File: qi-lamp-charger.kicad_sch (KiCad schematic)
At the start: 80 parts, among them J1 Conn_01x02, J2 Conn_01x02, J3 Conn_01x02, J4 Conn_01x06, J5 Conn_01x03, Q1 Q_PMOS_GDS, U1 SLG5NV1430V, U2 BQ51050BYFP, U3 ESP-12E

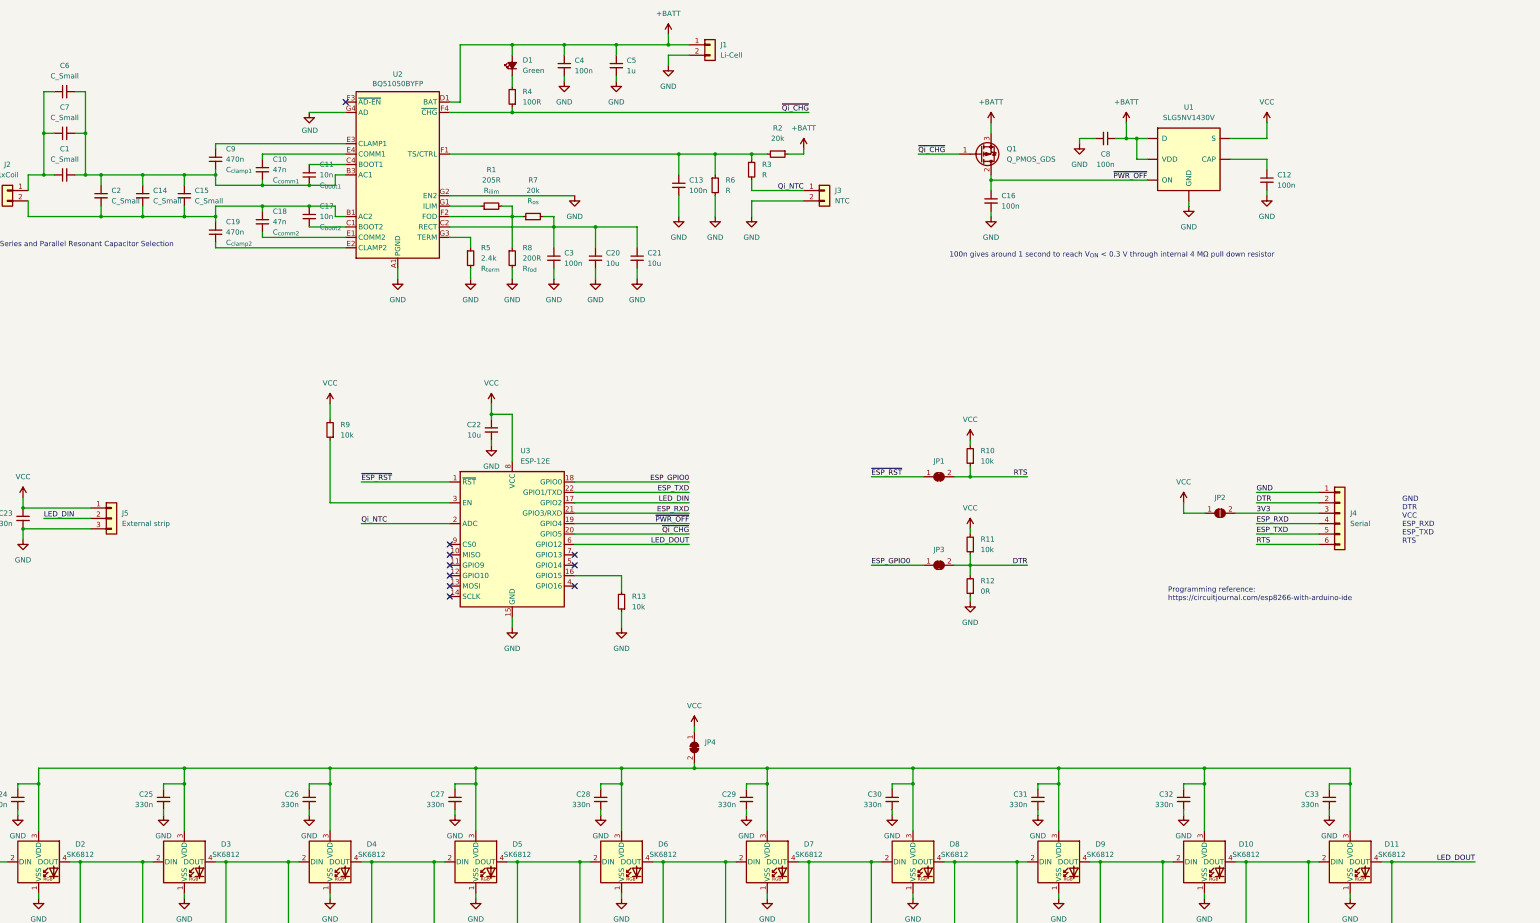
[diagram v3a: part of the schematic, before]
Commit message: Redraw Button/DTR/GPIO0 complex & assign footprints
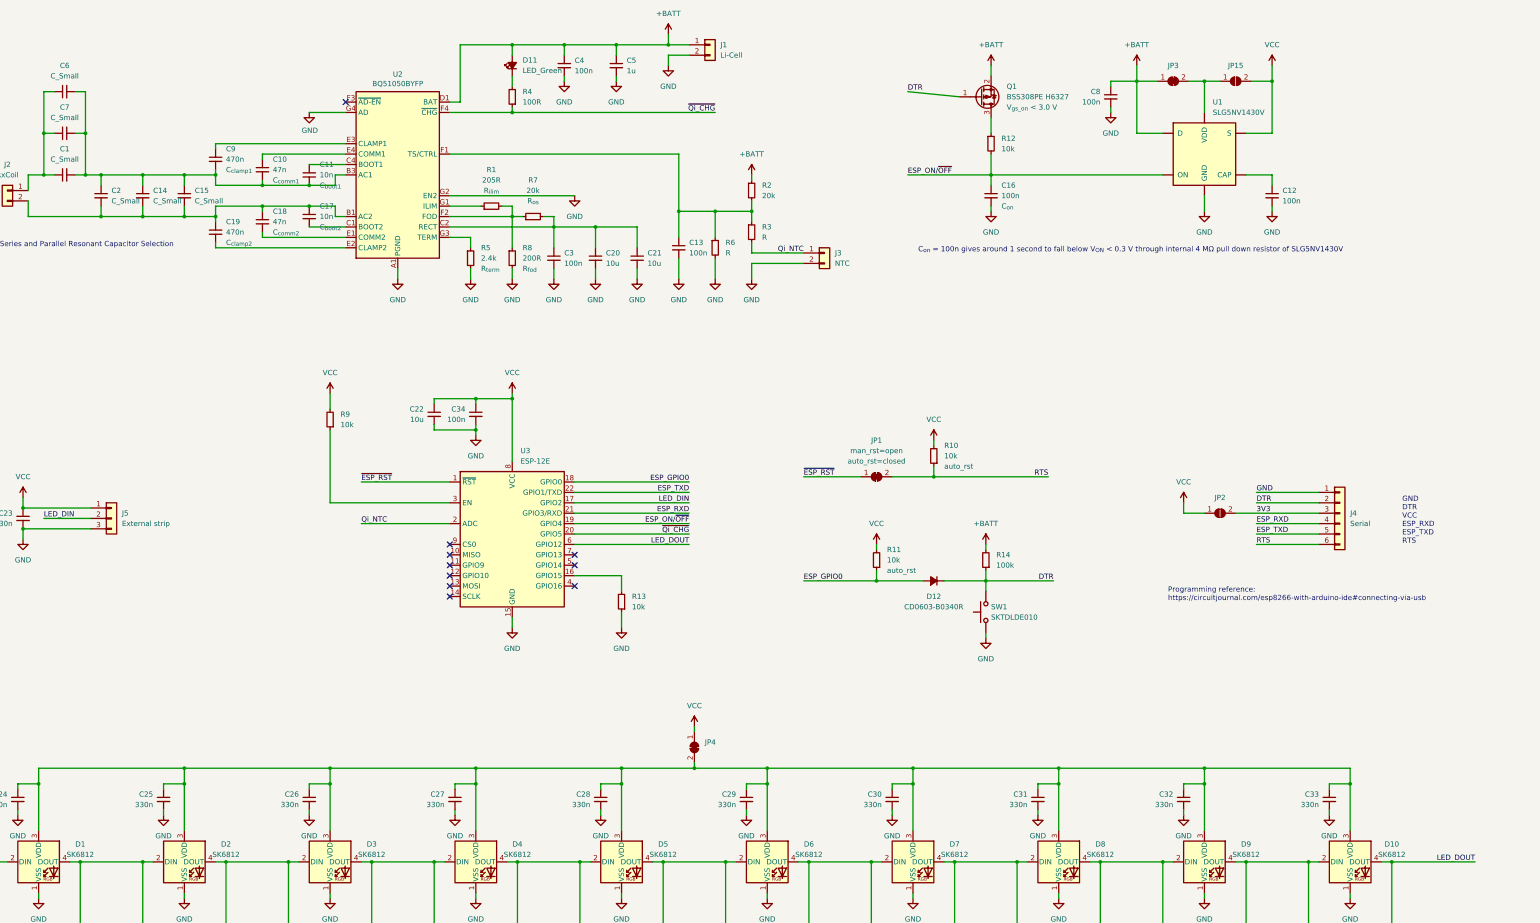
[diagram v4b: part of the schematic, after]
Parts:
- added C34: 100n, Capacitor_SMD:C_0603_1608Metric, symbol Device:C_Small
- added D12: CD0603-B0340R, Diode_SMD:D_0603_1608Metric, symbol Device:D_Small_Filled
- added JP15: SolderJumper_2_Open, Jumper:SolderJumper-2_P1.3mm_Open_RoundedPad1.0x1.5mm, symbol Jumper:SolderJumper_2_Open
- added R14: 100k, Resistor_SMD:R_0603_1608Metric, symbol Device:R_Small
- added SW1: SKTDLDE010, Kharars-KiCAD-lib:SKTDLDE010, symbol Switch:SW_Push
- C16: silk_text (none) -> C_{on}
- D11: renamed from D1; value Green -> LED_Green
- JP1: Rating (none) -> auto_rst=closed; silk_text (none) -> man_rst=open
- Q1: value Q_PMOS_GDS -> BSS308PE H6327; footprint (none) -> Package_TO_SOT_SMD:SOT-23; symbol Device:Q_PMOS_GDS -> Device:Q_PMOS_GSD; Rating (none) -> V_{gs_on} < 3.0 V
- R12: value 0R -> 10k; fit_field man_rst -> (none)
- U1: footprint (none) -> Kharars-KiCAD-lib:TDFN-8_1.5x2.0mm_P0.5mm (Fused Lead)
- renumbered D2 to D1, D11 to D10, D3 to D2, D4 to D3, D5 to D4, D6 to D5, D7 to D6, D8 to D7, D9 to D8, D10 to D9
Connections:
- net +BATT: now also JP3.1 (A), Q1.2 (S), R14.2; no longer Q1.3 (S), U1.1 (VDD)
- net DTR: now also Q1.1 (G), D12.1 (K), R14.1, SW1.2; no longer JP3.2 (B), R11.1, R12.2
- net ESP_GPIO0: now also R11.1, D12.2 (A); no longer JP3.1 (A)
- net GND: now also C34.2, SW1.1; no longer R12.1
- net VCC: now also C34.1, JP15.2 (B)
- net ~{Qi_CHG}: no longer Q1.1 (G)
- net ~{PWR_OFF} renamed ESP_ON/~{OFF}
- net ESP_ON/~{OFF}: now also R12.2; no longer Q1.2 (D)
- new net: JP15.1 (A), JP3.2 (B), U1.1 (VDD)
- new net: Q1.3 (D), R12.1
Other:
- note added: "C_{on} = 100n gives around 1 second to fall below V_{ON} < 0.3 V through internal 4 MΩ pull down resistor of SLG5NV1430V"
- note added: "Programming reference: https://circuitjournal.com/esp8266-with-arduino-ide#connecting-via-usb"
- note removed: "100n gives around 1 second to reach V_{ON} < 0.3 V through internal 4 MΩ pull down resistor"
- note removed: "Programming reference: https://circuitjournal.com/esp8266-with-arduino-ide"
- company: (none) -> Step 7 ApS
- title: (none) -> Main schematic
- moved on the sheet: C12, C13, C16, C22, C8, J3, Q1, R10, R11, R2, R3, R6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

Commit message: Layout proposal 1
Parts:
- C13: Name (none) -> C_{3}
- SW1: symbol Switch:SW_Push -> Kharars-KiCAD-lib:SW_Push
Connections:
- net GND: now also SW1.3
- net LED_VCC: now reaches C24.1, C25.1, C26.1, C27.1, C28.1, C29.1, C30.1, C31.1, C32.1, C33.1, D1.3 (VDD), D10.3 (VDD), D2.3 (VDD), D3.3 (VDD), D4.3 (VDD), D5.3 (VDD), D6.3 (VDD), D7.3 (VDD), D8.3 (VDD), D9.3 (VDD), JP4.2 (B)
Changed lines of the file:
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@@
     (stroke (width 0) (type default) (color 0 0 0 0))
   )
+  (wire (pts (xy 269.24 162.56) (xy 269.24 168.91))
+    (stroke (width 0) (type default) (color 0 0 0 0))
+  )
   (wire (pts (xy 344.17 135.89) (xy 359.41 135.89))
     (stroke (width 0) (type default) (color 0 0 0 0))
@@
     (stroke (width 0) (type default) (color 0 0 0 0))
   )
-  (wire (pts (xy 259.08 35.56) (xy 271.78 36.83))
+  (wire (pts (xy 259.08 36.83) (xy 271.78 36.83))
     (stroke (width 0) (type default) (color 0 0 0 0))
   )
@@
     (stroke (width 0) (type default) (color 0 0 0 0))
   )
+  (wire (pts (xy 273.05 162.56) (xy 269.24 162.56))
+    (stroke (width 0) (type default) (color 0 0 0 0))
+  )
   (wire (pts (xy 203.2 50.8) (xy 203.2 64.77))
     (stroke (width 0) (type default) (color 0 0 0 0))
@@
     (effects (font (size 1.27 1.27)) (justify left bottom))
   )
-  (label "DTR" (at 259.08 35.56 0)
+  (label "DTR" (at 259.08 36.83 0)
     (effects (font (size 1.27 1.27)) (justify left bottom))
   )
@@
     (effects (font (size 1.27 1.27)) (justify right bottom))
   )
+  (label "LED_VCC" (at 213.36 200.66 0)
+    (effects (font (size 1.27 1.27)) (justify left bottom))
+  )
   (label "~{Qi_CHG}" (at 205.74 143.51 180)
     (effects (font (size 1.27 1.27)) (justify right bottom))
@@
     (pin "1")
   )
+  (symbol (lib_id "power:GND") (at 269.24 168.91 0) (mirror y) (unit 1)
+    (in_bom yes) (on_board yes) (fields_autoplaced)
+    (property "Reference" "#PWR?" (id 0) (at 269.24 175.26 0)
+      (effects (font (size 1.27 1.27)) hide)
+    )
+    (property "Value" "GND" (id 1) (at 269.24 173.99 0))
+    (property "Footprint" "" (id 2) (at 269.24 168.91 0)
+      (effects (font (size 1.27 1.27)) hide)
+    )
+    (property "Datasheet" "" (id 3) (at 269.24 168.91 0)
+      (effects (font (size 1.27 1.27)) hide)
+    )
+    (pin "1")
+  )
   (symbol (lib_id "power:GND") (at 182.88 81.28 0) (unit 1)
     (in_bom yes) (on_board yes) (fields_autoplaced)
@@
     (pin "2")
   )
-  (symbol (lib_id "Switch:SW_Push") (at 278.13 162.56 90) (unit 1)
+  (symbol (lib_id "Kharars-KiCAD-lib:SW_Push") (at 278.13 162.56 270) (mirror x) (unit 1)
     (in_bom yes) (on_board yes) (fields_autoplaced)
-    (property "Reference" "SW1" (id 0) (at 279.4 161.2899 90)
-      (effects (font (size 1.27 1.27)) (justify right))
+    (property "Reference" "SW1" (id 0) (at 283.21 161.2899 90)
+      (effects (font (size 1.27 1.27)) (justify left))
     )
-    (property "Value" "SKTDLDE010" (id 1) (at 279.4 163.8299 90)
-      (effects (font (size 1.27 1.27)) (justify right))
+    (property "Value" "SKTDLDE010" (id 1) (at 283.21 163.8299 90)
+      (effects (font (size 1.27 1.27)) (justify left))
     )
-    (property "Footprint" "Kharars-KiCAD-lib:SKTDLDE010" (id 2) (at 273.05 162.56 0)
+    (property "Footprint" "Kharars-KiCAD-lib:SKTDLDE010" (id 2) (at 283.21 162.56 0)
       (effects (font (size 1.27 1.27)) hide)
     )
-    (property "Datasheet" "~" (id 3) (at 273.05 162.56 0)
+    (property "Datasheet" "~" (id 3) (at 283.21 162.56 0)
       (effects (font (size 1.27 1.27)) hide)
     )
     (pin "1")
     (pin "2")
+    (pin "3")
   )
   (symbol (lib_id "power:GND") (at 82.55 232.41 0) (unit 1)
@@
   (symbol (lib_id "Device:C_Small") (at 203.2 73.66 0) (unit 1)
     (in_bom yes) (on_board yes) (fields_autoplaced)
-    (property "Reference" "C13" (id 0) (at 205.74 72.3962 0)
+    (property "Reference" "C13" (id 0) (at 205.74 71.1262 0)
       (effects (font (size 1.27 1.27)) (justify left))
     )
-    (property "Value" "100n" (id 1) (at 205.74 74.9362 0)
+    (property "Value" "100n" (id 1) (at 205.74 73.6662 0)
       (effects (font (size 1.27 1.27)) (justify left))
     )
@@
       (effects (font (size 1.27 1.27)) hide)
     )
+    (property "Name" "C_{3}" (id 4) (at 205.74 76.2062 0)
+      (effects (font (size 1.27 1.27)) (justify left))
+    )
     (pin "1")
     (pin "2")
@@
       (reference "#PWR056") (unit 1) (value "+BATT") (footprint "")
     )
+    (path "/5c49c5da-cd36-4279-b071-c3b1b9b3257f"
+      (reference "#PWR?") (unit 1) (value "GND") (footprint "")
+    )
     (path "/3a78c529-0783-4f01-b00d-70d6f645ba2d"
